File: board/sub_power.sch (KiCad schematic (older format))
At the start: 0 parts

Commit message: More progress on the schematic. 6502 Done.
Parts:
- added U201: XC3S200-TQ144, symbol quokka:XC3S200-TQ144
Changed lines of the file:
@@
 $Descr A4 11693 8268
 encoding utf-8
-Sheet 1 8
+Sheet 2 10
 Title ""
 Date ""
@@
 Comment4 ""
 $EndDescr
+$Comp
+L quokka:XC3S200-TQ144 U201
+U 9 1 5AA358A2
+P 4150 3000
+F 0 "U201" H 4006 3915 50  0000 C CNN
+F 1 "XC3S200-TQ144" H 4006 3824 50  0000 C CNN
+F 2 "" H 3700 3100 50  0001 C CNN
+F 3 "" H 3700 3100 50  0001 C CNN
+	9    4150 3000
+	1    0    0    -1
+$EndComp
+$Comp
+L quokka:XC3S200-TQ144 U201
+U 11 1 5AA358F8
+P 6550 3000
+F 0 "U201" H 6231 3915 50  0000 C CNN
+F 1 "XC3S200-TQ144" H 6231 3824 50  0000 C CNN
+F 2 "" H 6100 3100 50  0001 C CNN
+F 3 "" H 6100 3100 50  0001 C CNN
+	11   6550 3000
+	1    0    0    -1
+$EndComp
 $EndSCHEMATC

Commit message: More schematic progress
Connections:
- net +3V3: now reaches U201.106 (VCCO_RIGHT)
- net +3V3: now also U201.115 (VCCO_TOP), U201.120 (VCCAUX), U201.126 (VCCO_TOP), U201.134 (VCCAUX), U201.138 (VCCO_TOP), U201.19 (VCCO_LEFT), U201.3 (VCCO_LEFT), U201.34 (VCCO_LEFT), U201.43 (VCCO_BOTTOM), U201.48 (VCCAUX), U201.54 (VCCO_BOTTOM), U201.62 (VCCAUX), U201.66 (VCCO_BOTTOM), U201.75 (VCCO_RIGHT), U201.91 (VCCO_RIGHT)
- net GND: now reaches U201.101 (GND)
- net GND: now also U201.114 (GND), U201.117 (GND), U201.136 (GND), U201.139 (GND), U201.16 (GND), U201.22 (GND), U201.29 (GND), U201.42 (GND), U201.45 (GND), U201.64 (GND), U201.67 (GND), U201.81 (GND), U201.88 (GND), U201.9 (GND), U201.94 (GND)
- net +1V2: now reaches U201.121 (VCCINT)
- net +1V2: now also U201.133 (VCCINT), U201.49 (VCCINT), U201.61 (VCCINT)
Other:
- moved on the sheet: U201I, U201K

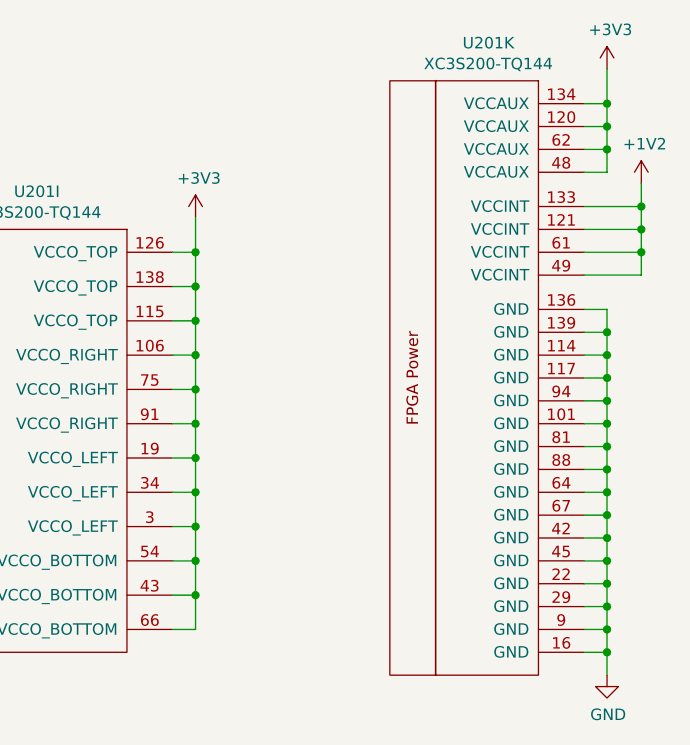
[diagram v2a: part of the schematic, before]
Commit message: Level converters complete, display almost done
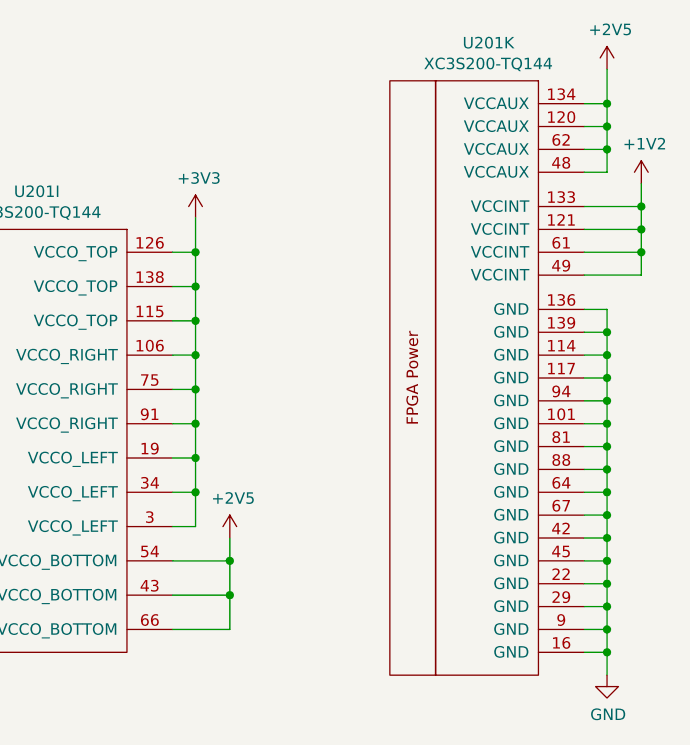
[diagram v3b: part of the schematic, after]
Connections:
- net +3V3: no longer U201.120 (VCCAUX), U201.134 (VCCAUX), U201.43 (VCCO_BOTTOM), U201.48 (VCCAUX), U201.54 (VCCO_BOTTOM), U201.62 (VCCAUX), U201.66 (VCCO_BOTTOM)
- new net +2V5: U201.120 (VCCAUX), U201.134 (VCCAUX), U201.43 (VCCO_BOTTOM), U201.48 (VCCAUX), U201.54 (VCCO_BOTTOM), U201.62 (VCCAUX), U201.66 (VCCO_BOTTOM)

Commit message: Schematics mostly complete
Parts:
- added C201, C206: 22n, symbol Device:C_Small
- added C202, C203: 1n, symbol Device:C_Small
- added C204: 68u, symbol Device:CP1
- added C205, C210: 10u, symbol Device:C
- added C207, C208, C211, C212: 22u, symbol Device:C
- added C209, C213: 100u, symbol Device:CP1
- added C214, C216, C219, C220, C221, C223, C224, C225, C227, C228, C229, C231, C232, C233, C234, C236, C238, C240, C242, C244, C246, C248: 1u, symbol Device:C
- added C215, C217, C218, C222, C226, C230: 4.7u, symbol Device:C
- added C235, C237, C239, C241, C243, C245, C247, C249: 0.1u, symbol Device:C
- added D201: D_TVS, symbol Device:D_TVS
- added F201: Polyfuse, symbol Device:Polyfuse
- added J201: Barrel_Jack, symbol Connector_Specialized:Barrel_Jack
- added L201: L_Coupled, symbol Device:L_Coupled
- added L202, L203: 4.7u, symbol Device:L
- added Q201: Q_PMOS_GSD, symbol Device:Q_PMOS_GSD
- added R201: 150, symbol Device:R
- added U201, U202: TS3001x, symbol quokka:TS3001x
- added U203: LDL1117S25R, symbol Regulator_Linear:TLV1117-33
- added U204: LDL1117S12R, symbol Regulator_Linear:TLV1117-33
- renumbered U201 to U205
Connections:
- net +1V2: now also C217.1, C242.1, C243.1, C244.1, C245.1, C246.1, C247.1, C248.1, C249.1, U204.2 (VO)
- net +2V5: now also C215.1, C216.1, C234.1, C235.1, C236.1, C237.1, C238.1, C239.1, C240.1, C241.1, R201.1, U203.2 (VO), U204.3 (VI); no longer U205.43 (VCCO_BOTTOM), U205.54 (VCCO_BOTTOM), U205.66 (VCCO_BOTTOM)
- net +3V3: now also U205.43 (VCCO_BOTTOM), U205.54 (VCCO_BOTTOM), U205.66 (VCCO_BOTTOM), C211.1, C212.1, C213.1, C214.1, C218.1, C219.1, C220.1, C221.1, C222.1, C223.1, C224.1, C225.1, C226.1, C227.1, C228.1, C229.1, C230.1, C231.1, C232.1, C233.1, L203.2, U202.5 (FB), U203.3 (VI)
- net GND: now also C204.2, C205.2, C207.2, C208.2, C209.2, C210.2, C211.2, C212.2, C213.2, C214.2, C215.2, C216.2, C217.2, C218.2, C219.2, C220.2, C221.2, C222.2, C223.2, C224.2, C225.2, C226.2, C227.2, C228.2, C229.2, C230.2, C231.2, C232.2, C233.2, C234.2, C235.2, C236.2, C237.2, C238.2, C239.2, C240.2, C241.2, C242.2, C243.2, C244.2, C245.2, C246.2, C247.2, C248.2, C249.2, L201.4, Q201.1 (G), R201.2, U201.14 (PGND), U201.15 (PGND), U201.17 (GND), U201.4 (GND), U202.14 (PGND), U202.15 (PGND), U202.17 (GND), U202.4 (GND), U203.1 (GND), U204.1 (GND)
- new net: C201.2, L202.1, U201.1 (VSW), U201.12 (VSW), U201.13 (VSW), U201.16 (VSW)
- new net: C201.1, U201.10 (BST)
- new net: C204.1, C205.1, Q201.2 (S), U201.11 (VCC), U201.2 (VCC), U201.3 (VCC)
- new net: L201.2, Q201.3 (D)
- new net: C202.1, C203.1, F201.2, J201.1
- new net: C202.2, C203.2, D201.2 (A2), J201.2, J201.3, L201.3
- new net: D201.1 (A1), F201.1, L201.1
- new net: C206.2, L203.1, U202.1 (VSW), U202.12 (VSW), U202.13 (VSW), U202.16 (VSW)
- new net: C206.1, U202.10 (BST)
- new net +5V: C207.1, C208.1, C209.1, C210.1, L202.2, U201.5 (FB), U202.11 (VCC), U202.2 (VCC), U202.3 (VCC)
- no-connect marks 0 -> 4
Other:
- moved on the sheet: U205I, U205K

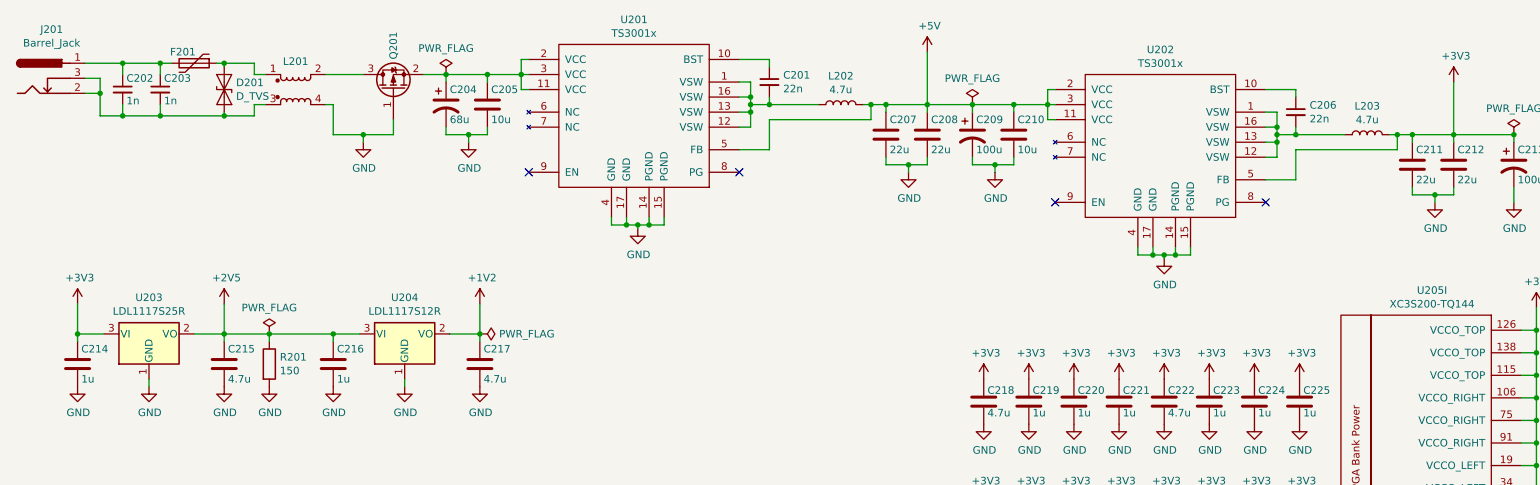
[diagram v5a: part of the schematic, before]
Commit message: Started picking footprints. Merged many components.
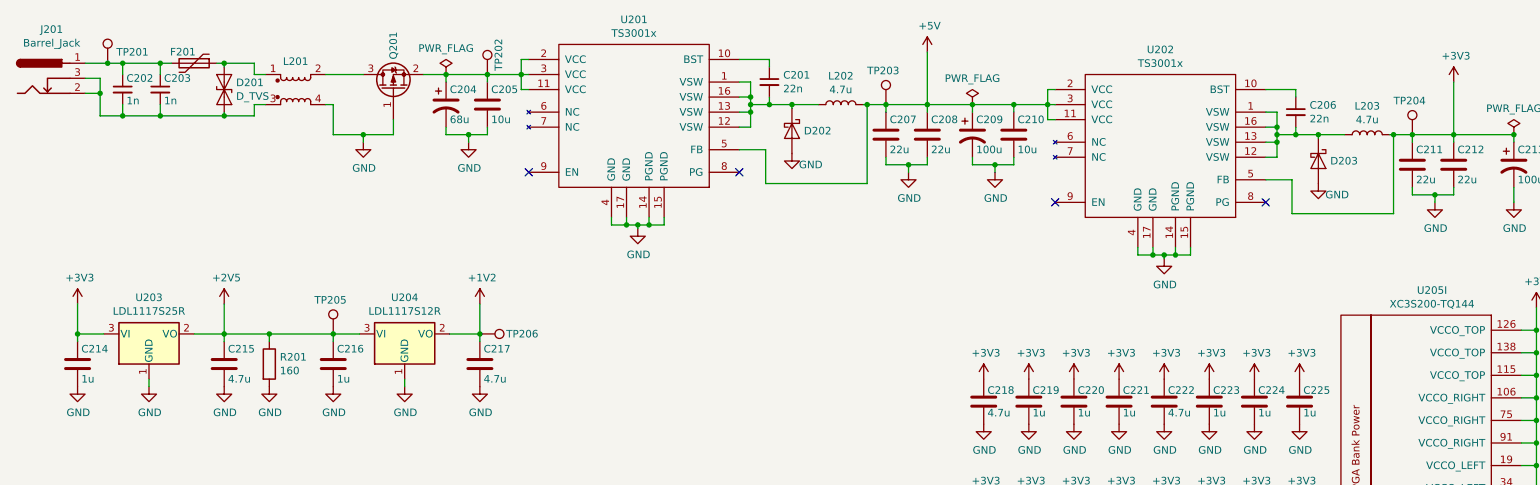
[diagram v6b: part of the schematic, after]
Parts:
- added D202, D203: D_Schottky, symbol Device:D_Schottky
- added TP201, TP202, TP203, TP204, TP205, TP206: Test_Point, TestPoint:TestPoint_Plated_Hole_D2.0mm, symbol Connector_Specialized:Test_Point
- R201: value 150 -> 160
- U201, U202: footprint (none) -> Package_DFN_QFN:UQFN-16-1EP_3x3mm_P0.5mm_EP1.75x1.75mm
- U203, U204: footprint (none) -> Package_TO_SOT_SMD:SOT-223-3_TabPin2
- U205: footprint (none) -> Package_QFP:LQFP-144_20x20mm_P0.5mm
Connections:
- net +1V2: now also TP206.1
- net +2V5: now also TP205.1
- net +3V3: now also TP204.1
- net +5V: now also TP203.1
- net GND: now also D202.2 (A), D203.2 (A)
- net at C201.2, L202.1, U201.1 (VSW)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: now also D202.1 (K)
- net at C204.1, C205.1, Q201.2 (S)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: now also TP202.1
- net at C202.1, C203.1, F201.2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: now also TP201.1
- net at C206.2, L203.1, U202.1 (VSW)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: now also D203.1 (K)

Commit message: More footprints done. Went with simpler test-pads.
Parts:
- F201: footprint (none) -> Fuse:Fuse_2920_7451Metric
- J201: footprint (none) -> Connector_BarrelJack:BarrelJack_CUI_PJ-102AH_Horizontal
- Q201: footprint (none) -> Package_TO_SOT_SMD:SOT-23
- R201: footprint (none) -> Resistor_SMD:R_1206_3216Metric
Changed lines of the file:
@@
 $Descr A4 11693 8268
 encoding utf-8
-Sheet 2 15
+Sheet 2 14
 Title ""
 Date ""
@@
 F 0 "Q201" H 3300 975 50  0000 L CNN
 F 1 "Q_PMOS_GSD" H 3306 930 50  0001 L CNN
-F 2 "" H 3300 1075 50  0001 C CNN
+F 2 "Package_TO_SOT_SMD:SOT-23" H 3300 1075 50  0001 C CNN
 F 3 "~" H 3100 975 50  0001 C CNN
 	1    3100 975
@@
 F 0 "J201" H 828 1225 50  0000 C CNN
 F 1 "Barrel_Jack" H 828 1134 50  0000 C CNN
-F 2 "" H 800 860 50  0001 C CNN
+F 2 "Connector_BarrelJack:BarrelJack_CUI_PJ-102AH_Horizontal" H 800 860 50  0001 C CNN
 F 3 "~" H 800 860 50  0001 C CNN
 	1    750  900
@@
 F 0 "F201" V 1700 725 50  0000 C CNN
 F 1 "Polyfuse" V 1641 800 50  0001 C CNN
-F 2 "" H 1825 600 50  0001 L CNN
+F 2 "Fuse:Fuse_2920_7451Metric" H 1825 600 50  0001 L CNN
 F 3 "~" H 1775 800 50  0001 C CNN
 	1    1775 800
@@
 F 0 "R201" H 2345 2846 50  0000 L CNN
 F 1 "160" H 2345 2755 50  0000 L CNN
-F 2 "" V 2205 2800 50  0001 C CNN
+F 2 "Resistor_SMD:R_1206_3216Metric" V 2205 2800 50  0001 C CNN
 F 3 "~" H 2275 2800 50  0001 C CNN
 	1    2275 2800
